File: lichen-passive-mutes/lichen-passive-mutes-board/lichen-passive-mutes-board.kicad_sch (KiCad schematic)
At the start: 9 parts, among them J1 Eurorack_Mono_Jack, J2 Eurorack_Mono_Jack, J3 Eurorack_Mono_Jack, J4 Eurorack_Mono_Jack, J5 Eurorack_Mono_Jack, J6 Eurorack_Mono_Jack, SW1 SW_SPDT, SW2 SW_SPDT, SW3 SW_SPDT

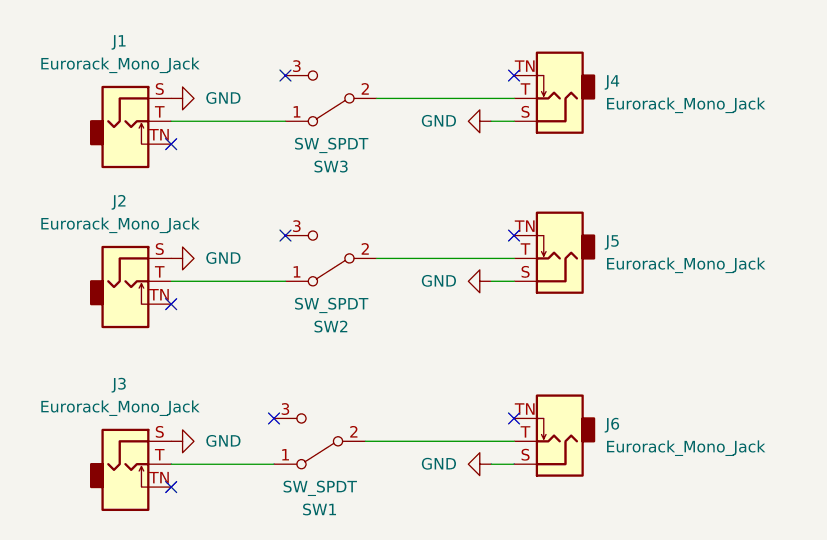
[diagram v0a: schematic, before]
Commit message: Fixes connections between jacks and switches on Lichen Sw. Now the panel is laid out so channels 1-3 are laid out sequentially.
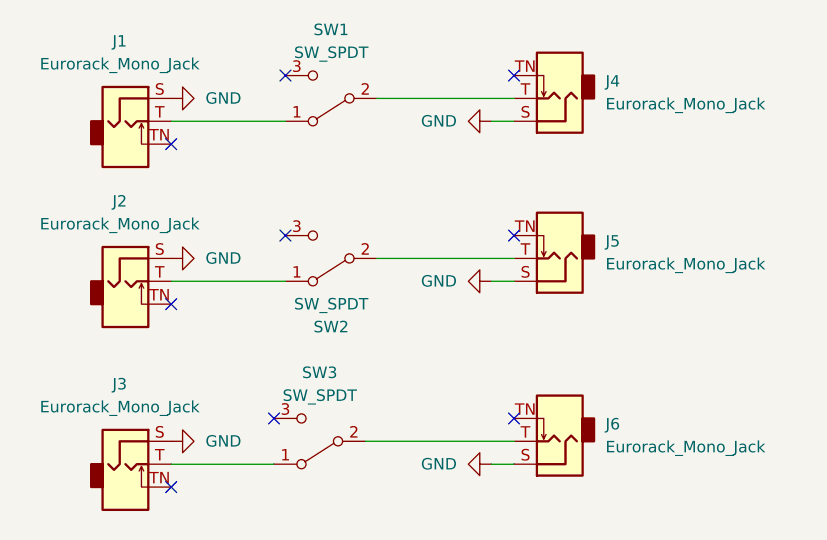
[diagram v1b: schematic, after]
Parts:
- renumbered SW3 to SW1, SW1 to SW3
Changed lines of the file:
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@@
     (pin "1")
     (instances
-      (project "lichen-passive-mutes"
+      (project "lichen-passive-mutes-board"
         (path "/1ae5b669-8542-4edb-8110-fc9c765afc0e"
           (reference "#PWR01") (unit 1)
@@
   (symbol (lib_id "Switch:SW_SPDT") (at 82.55 105.41 180) (unit 1)
     (in_bom yes) (on_board yes) (dnp no) (fields_autoplaced)
-    (property "Reference" "SW1" (at 82.55 113.03 0)
-      (effects (font (size 1.27 1.27)))
-    )
-    (property "Value" "SW_SPDT" (at 82.55 110.49 0)
+    (property "Reference" "SW3" (at 82.55 97.79 0)
+      (effects (font (size 1.27 1.27)))
+    )
+    (property "Value" "SW_SPDT" (at 82.55 100.33 0)
       (effects (font (size 1.27 1.27)))
     )
@@
     (pin "3")
     (instances
-      (project "lichen-passive-mutes"
-        (path "/1ae5b669-8542-4edb-8110-fc9c765afc0e"
-          (reference "SW1") (unit 1)
+      (project "lichen-passive-mutes-board"
+        (path "/1ae5b669-8542-4edb-8110-fc9c765afc0e"
+          (reference "SW3") (unit 1)
         )
       )
@@
     (pin "TN")
     (instances
-      (project "lichen-passive-mutes"
+      (project "lichen-passive-mutes-board"
         (path "/1ae5b669-8542-4edb-8110-fc9c765afc0e"
           (reference "J1") (unit 1)
@@
     (pin "1")
     (instances
-      (project "lichen-passive-mutes"
+      (project "lichen-passive-mutes-board"
         (path "/1ae5b669-8542-4edb-8110-fc9c765afc0e"
           (reference "#PWR02") (unit 1)
@@
     (pin "1")
     (instances
-      (project "lichen-passive-mutes"
+      (project "lichen-passive-mutes-board"
         (path "/1ae5b669-8542-4edb-8110-fc9c765afc0e"
           (reference "#PWR06") (unit 1)
@@
     (pin "1")
     (instances
-      (project "lichen-passive-mutes"
+      (project "lichen-passive-mutes-board"
         (path "/1ae5b669-8542-4edb-8110-fc9c765afc0e"
           (reference "#PWR04") (unit 1)
@@
   (symbol (lib_id "Switch:SW_SPDT") (at 83.82 67.31 180) (unit 1)
     (in_bom yes) (on_board yes) (dnp no) (fields_autoplaced)
-    (property "Reference" "SW3" (at 83.82 74.93 0)
-      (effects (font (size 1.27 1.27)))
-    )
-    (property "Value" "SW_SPDT" (at 83.82 72.39 0)
+    (property "Reference" "SW1" (at 83.82 59.69 0)
+      (effects (font (size 1.27 1.27)))
+    )
+    (property "Value" "SW_SPDT" (at 83.82 62.23 0)
       (effects (font (size 1.27 1.27)))
     )
@@
     (pin "3")
     (instances
-      (project "lichen-passive-mutes"
-        (path "/1ae5b669-8542-4edb-8110-fc9c765afc0e"
-          (reference "SW3") (unit 1)
+      (project "lichen-passive-mutes-board"
+        (path "/1ae5b669-8542-4edb-8110-fc9c765afc0e"
+          (reference "SW1") (unit 1)
         )
       )
@@
     (pin "1")
     (instances
-      (project "lichen-passive-mutes"
+      (project "lichen-passive-mutes-board"
         (path "/1ae5b669-8542-4edb-8110-fc9c765afc0e"
           (reference "#PWR05") (unit 1)
@@
     (pin "TN")
     (instances
-      (project "lichen-passive-mutes"
+      (project "lichen-passive-mutes-board"
         (path "/1ae5b669-8542-4edb-8110-fc9c765afc0e"
           (reference "J2") (unit 1)
@@
     (pin "1")
     (instances
-      (project "lichen-passive-mutes"
+      (project "lichen-passive-mutes-board"
         (path "/1ae5b669-8542-4edb-8110-fc9c765afc0e"
           (reference "#PWR03") (unit 1)
@@
     (pin "3")
     (instances
-      (project "lichen-passive-mutes"
+      (project "lichen-passive-mutes-board"
         (path "/1ae5b669-8542-4edb-8110-fc9c765afc0e"
           (reference "SW2") (unit 1)
@@
     (pin "TN")
     (instances
-      (project "lichen-passive-mutes"
+      (project "lichen-passive-mutes-board"
         (path "/1ae5b669-8542-4edb-8110-fc9c765afc0e"
           (reference "J6") (unit 1)
@@
     (pin "TN")
     (instances
-      (project "lichen-passive-mutes"
+      (project "lichen-passive-mutes-board"
         (path "/1ae5b669-8542-4edb-8110-fc9c765afc0e"
           (reference "J4") (unit 1)
@@
     (pin "TN")
     (instances
-      (project "lichen-passive-mutes"
+      (project "lichen-passive-mutes-board"
         (path "/1ae5b669-8542-4edb-8110-fc9c765afc0e"
           (reference "J3") (unit 1)
@@
     (pin "TN")
     (instances
-      (project "lichen-passive-mutes"
+      (project "lichen-passive-mutes-board"
         (path "/1ae5b669-8542-4edb-8110-fc9c765afc0e"
           (reference "J5") (unit 1)
